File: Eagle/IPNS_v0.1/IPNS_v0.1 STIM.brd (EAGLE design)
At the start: 32.7 x 33 mm, 19 parts, among them J1 OUTPUT CONN, J2 POL SWITCH CONN, J3 LEFT CONN, J4 RIGHT CONN, U1 LTC3459ES6TRMPBF, U2 LT1492CS8TRPBF

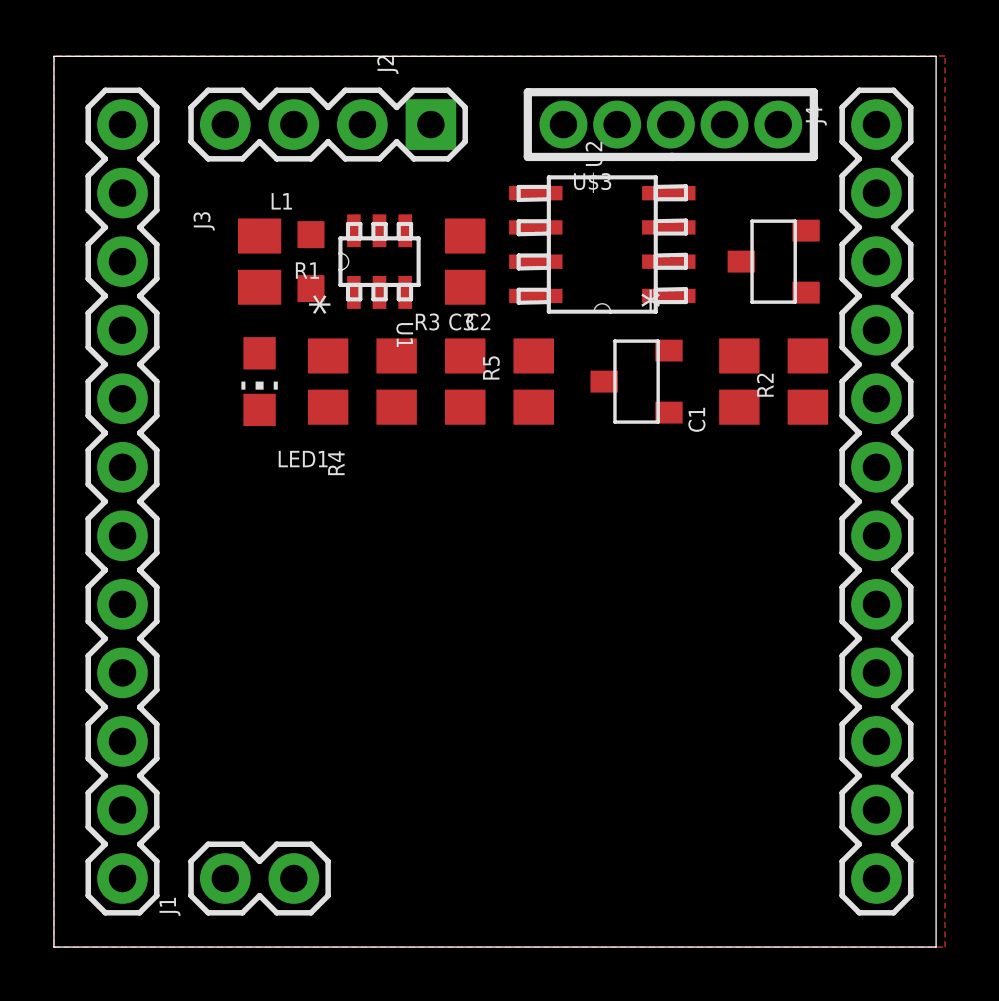
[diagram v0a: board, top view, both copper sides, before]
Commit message: Routed everything; no DRC errors other than Stop Mask
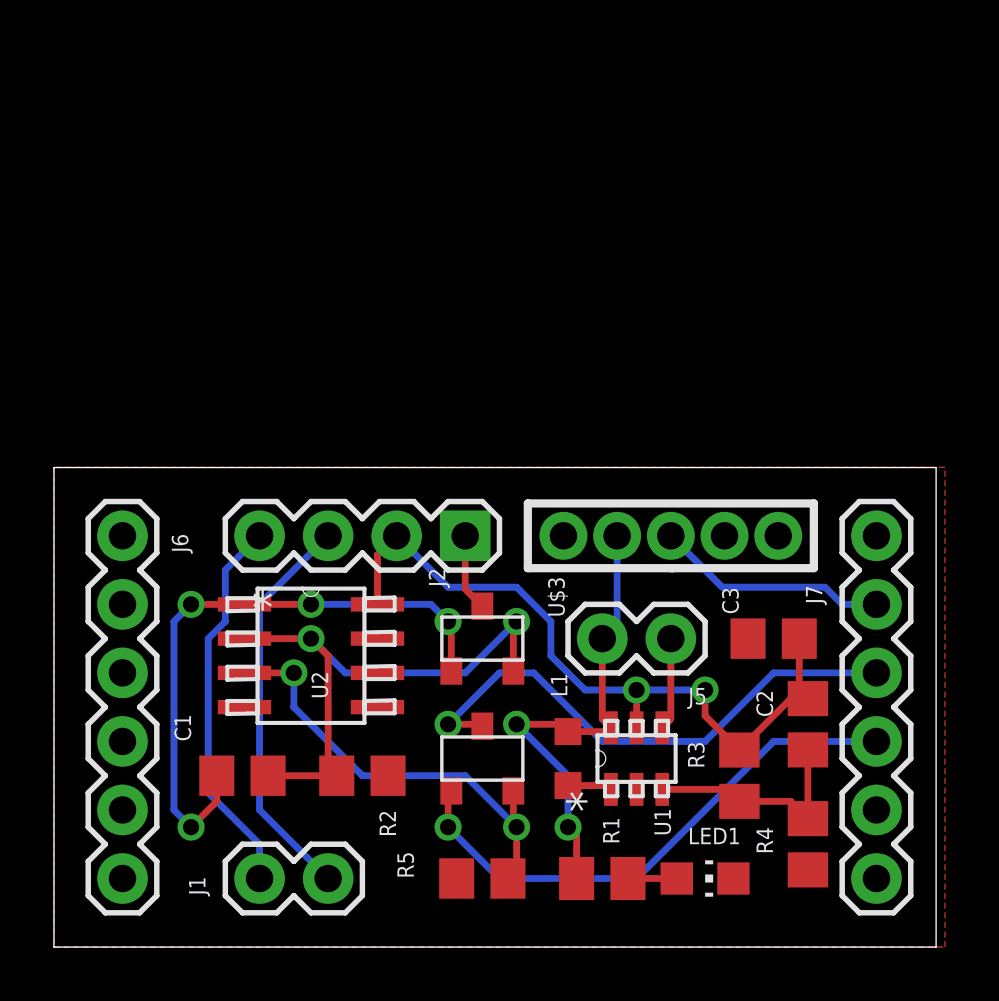
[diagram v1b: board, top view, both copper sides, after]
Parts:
- removed J3: LEFT CONN, IPNS_Lib_v0.1:1X12
- removed J4: RIGHT CONN, IPNS_Lib_v0.1:1X12
- added J5: (no value), IPNS_Lib_v0.1:1X02
- added J6, J7: (no value), IPNS_Lib_v0.1:1X06
- moved R1 26.2 mm to (20.3, 2.54), turned to 0 degrees
- moved LED1 24.7 mm to (24.1, 2.54), turned to 270 degrees
- moved R4 24.7 mm to (27.9, 3.81)
- moved C1 23.5 mm to (6.99, 6.35), turned to 0 degrees
- moved R2 22.0 mm to (11.4, 6.35), turned to 180 degrees
- moved U$2 21.3 mm to (15.9, 6.99), turned to 90 degrees
- moved L1 20.7 mm to (19.1, 6.99)
- moved U1 20.7 mm to (21.6, 6.99)
- moved R3 19.4 mm to (25.4, 6.35), turned to 90 degrees
- moved U2 18.7 mm to (9.53, 10.8), turned to 0 degrees
- moved R5 18.5 mm to (15.9, 2.54), turned to 0 degrees
- moved C3 18.1 mm to (26.7, 11.4), turned to 180 degrees
- moved C2 18.0 mm to (27.9, 8.26), turned to 90 degrees
- moved J2 15.3 mm to (15.2, 15.2)
- moved U$3 15.2 mm to (22.9, 15.2)
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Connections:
- removed net N$10: J3.6
- removed net N$11: J3.7
- removed net N$12: J3.8
- removed net N$13: J3.9
- removed net N$14: J3.10
- removed net N$15: J3.11
- removed net N$18: J4.11
- removed net N$19: J4.10
- removed net N$20: J4.9
- removed net N$21: J4.8
- removed net N$22: J4.7
- removed net N$23: J4.6
- removed net N$24: J4.5
- removed net N$7: J3.3
- removed net N$8: J3.4
- removed net N$9: J3.5
- new net N$25: J6.5
- new net N$26: J6.4
- new net N$27: J6.3
- new net N$29: J7.5
- new net N$30: J7.6
- new net SHDN: J5.1, U1.4
- net +3V3: now also J6.2; no longer J3.2
- net GND: now also J6.1, J6.6, J7.1; no longer J3.1, J3.12, J4.1, J4.12
- net VBATT: now also J7.2; no longer J4.2
- net VBOOST: now also J2.2; no longer J2.1
- net VCASE: now also J2.4; no longer J2.3
- net VDAC: now also J7.3; no longer J4.3
- net VELEC: now also J2.3; no longer J2.4
- net VLOW: now also J2.1; no longer J2.2
- net VON: now also J5.2; no longer U1.4
- net VPWM: now also J7.4; no longer J4.4
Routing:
- net VBOOST: track 0.00 -> 27.2 mm, vias 0 -> 2
- net N$2: track 0.00 -> 23.5 mm, vias 0 -> 4
- net N$4: track 0.00 -> 21.3 mm, vias 0 -> 2
- net VPWM: track 0.00 -> 20.2 mm, vias 0 -> 1
- net VDAC: track 0.00 -> 20.1 mm, vias 0 -> 1
- net VON: track 0.00 -> 17.8 mm, vias 0 -> 2
- net VIN: track 0.00 -> 16.6 mm, vias 0 -> 2
- net VELEC: track 0.00 -> 14.8 mm
- net VCASE: track 0.00 -> 14.3 mm
- net VBATT: track 0.00 -> 8.67 mm
- net N$5: track 0.00 -> 8.39 mm
- net SHDN: track 0.00 -> 3.43 mm
- net VLOW: track 0.00 -> 2.87 mm
- net N$1: track 0.00 -> 1.81 mm
- net N$6: track 0.00 -> 1.65 mm
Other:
- board size 32.7 x 33 mm -> 32.7 x 17.8 mm

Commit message: Broke out more pins on the MCU module
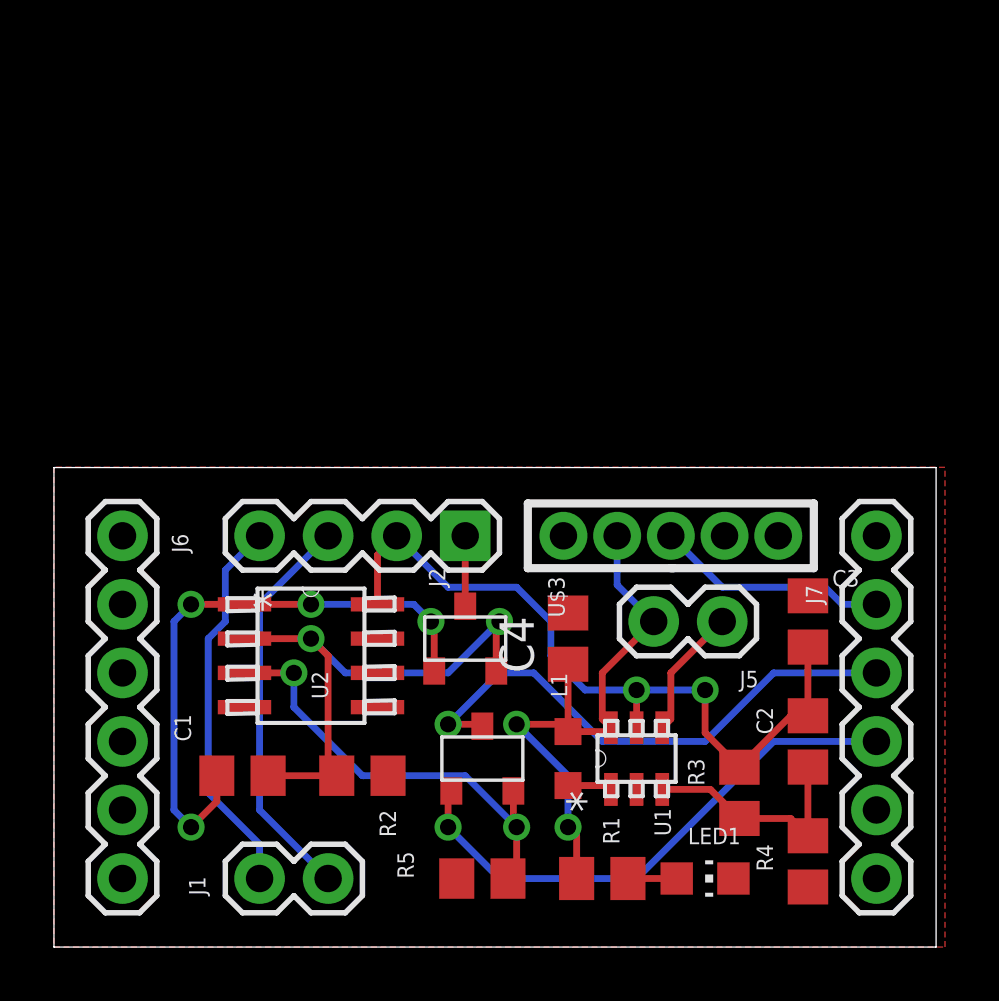
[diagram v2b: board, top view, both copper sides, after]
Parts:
- added C4: 1u, IPNS_Lib_v0.1:C0805
- L1: value 22uH -> 33uH
- moved J5 2.01 mm to (24.8, 12.1)
- moved C3 1.42 mm to (27.9, 12.1), turned to 90 degrees
- moved C2 0.64 mm to (27.9, 7.62)
- moved R4 0.64 mm to (27.9, 3.17)
- moved R3 0.63 mm to (25.4, 5.71)
- moved U$1 0.63 mm to (15.2, 11.4)
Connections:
- new net N$3: J6.6
- net GND: now also C4.2; no longer J6.6
- net VON: now also C4.1
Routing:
- net VON: track 17.8 -> 21.4 mm
- net SHDN: track 3.43 -> 4.86 mm
- net VBOOST: track 27.2 -> 28.0 mm
- net N$2: track 23.5 -> 22.8 mm
- net N$4: track 21.3 -> 20.7 mm

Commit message: Two PCBs clearances adjusted
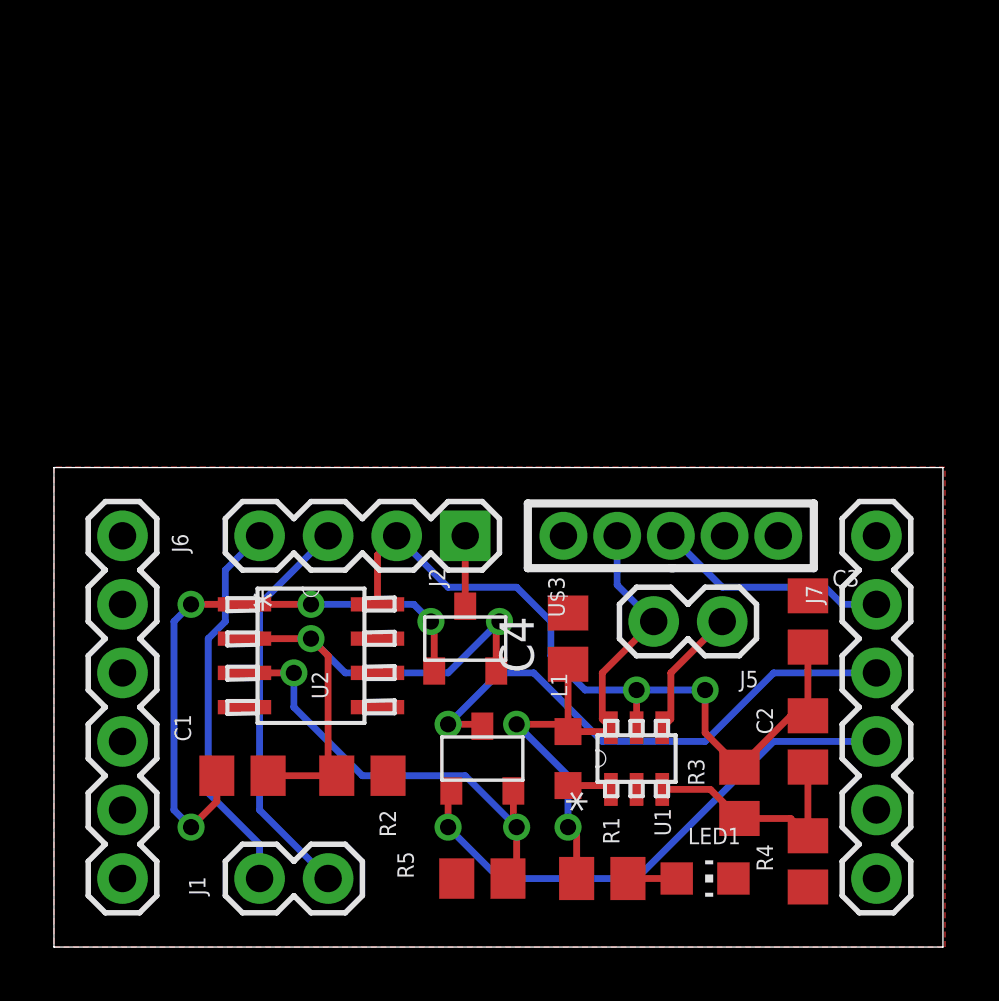
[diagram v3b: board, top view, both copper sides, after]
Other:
- board size 32.7 x 17.8 mm -> 32.9 x 17.8 mm
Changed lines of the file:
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@@
 <setting verticaltext="up"/>
 </settings>
-<grid distance="0.05" unitdist="inch" unit="inch" style="lines" multiple="1" display="yes" altdistance="0.025" altunitdist="inch" altunit="inch"/>
+<grid distance="0.05" unitdist="inch" unit="inch" style="lines" multiple="1" display="yes" altdistance="0.01" altunitdist="inch" altunit="inch"/>
 <layers>
 <layer number="1" name="Top" color="4" fill="1" visible="yes" active="yes"/>
@@
 <board>
 <plain>
-<wire x1="0" y1="0" x2="32.69" y2="0" width="0" layer="20"/>
-<wire x1="32.69" y1="0" x2="32.69" y2="17.77" width="0" layer="20"/>
-<wire x1="32.69" y1="17.77" x2="0" y2="17.77" width="0" layer="20"/>
+<wire x1="0" y1="0" x2="32.944" y2="0" width="0" layer="20"/>
+<wire x1="32.944" y1="0" x2="32.944" y2="17.77" width="0" layer="20"/>
+<wire x1="32.944" y1="17.77" x2="0" y2="17.77" width="0" layer="20"/>
 <wire x1="0" y1="17.77" x2="0" y2="0" width="0" layer="20"/>
 </plain>
@@
 <contactref element="U1" pad="2"/>
 <contactref element="R5" pad="1"/>
-<polygon width="0.4064" layer="1">
+<polygon width="0.254" layer="1" isolate="0.254">
 <vertex x="0" y="17.78"/>
 <vertex x="0" y="0"/>
